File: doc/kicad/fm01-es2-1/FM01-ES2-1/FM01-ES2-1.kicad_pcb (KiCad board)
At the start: 2 copper layers, 20 x 32 mm, 27 parts, among them J1 USB_B_Micro, J2 Conn_01x10, J3 Conn_01x10, J4 Conn_01x30, U1 ESP32-S2-WROVER-I

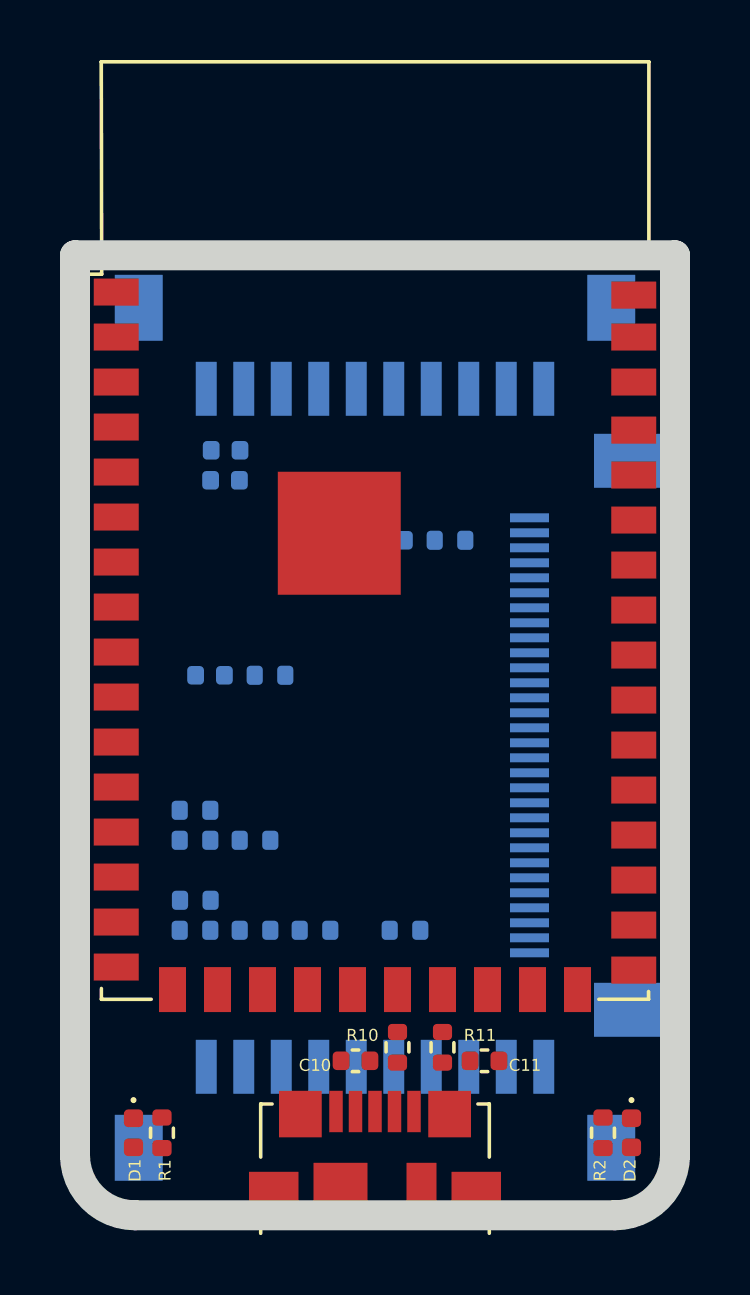
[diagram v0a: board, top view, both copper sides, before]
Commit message: doc/kicad: FM01-ES2-1  update PCB
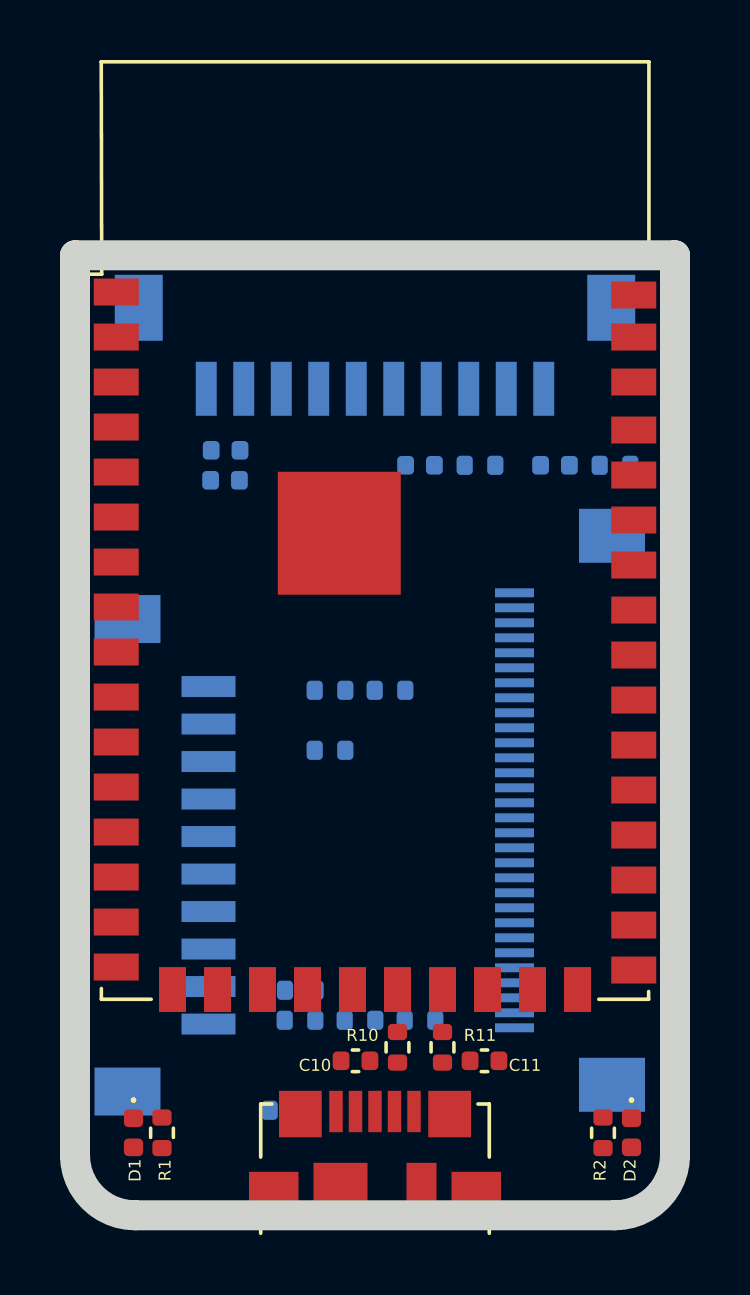
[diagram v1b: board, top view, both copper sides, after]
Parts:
- moved J3 11.0 mm to (183.0, 88.0), turned to 90 degrees
- moved C3 9.90 mm to (191.5, 75.0)
- moved R3 9.90 mm to (193.5, 75.0)
- moved R18 7.21 mm to (187.0, 96.5)
- moved R33 6.73 mm to (188.5, 82.5)
- moved R34 6.73 mm to (190.5, 82.5)
- moved C4 6.04 mm to (196.0, 75.0)
- moved R4 6.04 mm to (198.0, 75.0)
- moved R35 4.92 mm to (188.5, 84.5)
- moved R30 4.61 mm to (187.5, 93.5)
- moved R31 4.61 mm to (189.5, 93.5)
- moved R32 4.61 mm to (191.5, 93.5)
- moved R36 4.61 mm to (187.5, 92.5)
- moved J4 2.55 mm to (196.5, 86.5)
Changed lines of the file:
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@@
     (46 B.CrtYd user)
     (47 F.CrtYd user)
-    (48 B.Fab user hide)
-    (49 F.Fab user hide)
+    (48 B.Fab user)
+    (49 F.Fab user)
   )
   (setup
@@
   )
   (module Resistor_SMD:R_0402_1005Metric (layer B.Cu)
-    (at 184.01 89.5)
+    (at 187.51 92.5)
     (descr "Resistor SMD 0402 (1005 Metric), square (rectangular) end terminal, IPC_7351 nominal, (Body size source: IPC-SM-782 page 72, https://www.pcb-3d.com/wordpress/wp-content/uploads/ipc-sm-782a_amendment_1_and_2.pdf), generated with kicad-footprint-generator")
     (tags resistor)
     (attr smd)
-    (fp_text reference R36 (at -1.51 0) (layer B.SilkS)
+    (fp_text reference R36 (at -0.01 -1) (layer B.SilkS)
       (effects (font (size 0.4 0.4) (thickness 0.1)) (justify mirror))
     )
@@
   )
   (module Resistor_SMD:R_0402_1005Metric (layer B.Cu)
-    (at 184 86.5)
+    (at 188.5 84.5)
     (descr "Resistor SMD 0402 (1005 Metric), square (rectangular) end terminal, IPC_7351 nominal, (Body size source: IPC-SM-782 page 72, https://www.pcb-3d.com/wordpress/wp-content/uploads/ipc-sm-782a_amendment_1_and_2.pdf), generated with kicad-footprint-generator")
     (tags resistor)
     (attr smd)
-    (fp_text reference R35 (at 0 2) (layer B.SilkS)
+    (fp_text reference R35 (at 0 1) (layer B.SilkS)
       (effects (font (size 0.4 0.4) (thickness 0.1)) (justify mirror))
     )
@@
   )
   (module Resistor_SMD:R_0402_1005Metric (layer B.Cu)
-    (at 186 87.5 180)
+    (at 190.5 82.5 180)
     (descr "Resistor SMD 0402 (1005 Metric), square (rectangular) end terminal, IPC_7351 nominal, (Body size source: IPC-SM-782 page 72, https://www.pcb-3d.com/wordpress/wp-content/uploads/ipc-sm-782a_amendment_1_and_2.pdf), generated with kicad-footprint-generator")
     (tags resistor)
@@
   )
   (module Resistor_SMD:R_0402_1005Metric (layer B.Cu)
-    (at 184 87.5 180)
+    (at 188.5 82.5 180)
     (descr "Resistor SMD 0402 (1005 Metric), square (rectangular) end terminal, IPC_7351 nominal, (Body size source: IPC-SM-782 page 72, https://www.pcb-3d.com/wordpress/wp-content/uploads/ipc-sm-782a_amendment_1_and_2.pdf), generated with kicad-footprint-generator")
     (tags resistor)
     (attr smd)
-    (fp_text reference R33 (at 1.5 1) (layer B.SilkS)
+    (fp_text reference R33 (at 0 -1) (layer B.SilkS)
       (effects (font (size 0.4 0.4) (thickness 0.1)) (justify mirror))
     )
@@
   )
   (module Resistor_SMD:R_0402_1005Metric (layer B.Cu)
-    (at 188 90.5 180)
+    (at 191.5 93.5 180)
     (descr "Resistor SMD 0402 (1005 Metric), square (rectangular) end terminal, IPC_7351 nominal, (Body size source: IPC-SM-782 page 72, https://www.pcb-3d.com/wordpress/wp-content/uploads/ipc-sm-782a_amendment_1_and_2.pdf), generated with kicad-footprint-generator")
     (tags resistor)
@@
   )
   (module Resistor_SMD:R_0402_1005Metric (layer B.Cu)
-    (at 186 90.5 180)
+    (at 189.5 93.5 180)
     (descr "Resistor SMD 0402 (1005 Metric), square (rectangular) end terminal, IPC_7351 nominal, (Body size source: IPC-SM-782 page 72, https://www.pcb-3d.com/wordpress/wp-content/uploads/ipc-sm-782a_amendment_1_and_2.pdf), generated with kicad-footprint-generator")
     (tags resistor)
@@
   )
   (module Resistor_SMD:R_0402_1005Metric (layer B.Cu)
-    (at 184 90.5)
+    (at 187.5 93.5)
     (descr "Resistor SMD 0402 (1005 Metric), square (rectangular) end terminal, IPC_7351 nominal, (Body size source: IPC-SM-782 page 72, https://www.pcb-3d.com/wordpress/wp-content/uploads/ipc-sm-782a_amendment_1_and_2.pdf), generated with kicad-footprint-generator")
     (tags resistor)
@@
   )
   (module Resistor_SMD:R_0402_1005Metric (layer B.Cu)
-    (at 191 90.5)
+    (at 187 96.5)
     (descr "Resistor SMD 0402 (1005 Metric), square (rectangular) end terminal, IPC_7351 nominal, (Body size source: IPC-SM-782 page 72, https://www.pcb-3d.com/wordpress/wp-content/uploads/ipc-sm-782a_amendment_1_and_2.pdf), generated with kicad-footprint-generator")
     (tags resistor)
@@
   )
   (module Resistor_SMD:R_0402_1005Metric (layer B.Cu)
-    (at 192.5 77.5)
+    (at 198 75)
     (descr "Resistor SMD 0402 (1005 Metric), square (rectangular) end terminal, IPC_7351 nominal, (Body size source: IPC-SM-782 page 72, https://www.pcb-3d.com/wordpress/wp-content/uploads/ipc-sm-782a_amendment_1_and_2.pdf), generated with kicad-footprint-generator")
     (tags resistor)
@@
   )
   (module Resistor_SMD:R_0402_1005Metric (layer B.Cu)
-    (at 186.5 82)
+    (at 193.5 75)
     (descr "Resistor SMD 0402 (1005 Metric), square (rectangular) end terminal, IPC_7351 nominal, (Body size source: IPC-SM-782 page 72, https://www.pcb-3d.com/wordpress/wp-content/uploads/ipc-sm-782a_amendment_1_and_2.pdf), generated with kicad-footprint-generator")
     (tags resistor)
@@
   )
   (module Connector_FFC-FPC:Hirose_FH12-30S-0.5SH_1x30-1MP_P0.50mm_Horizontal (layer B.Cu)
-    (at 197 84 270)
+    (at 196.5 86.5 270)
     (descr "Hirose FH12, FFC/FPC connector, FH12-30S-0.5SH, 30 Pins per row (https://www.hirose.com/product/en/products/FH12/FH12-24S-0.5SH(55)/), generated with kicad-footprint-generator")
     (tags "connector Hirose FH12 horizontal")
@@
   )
   (module Connector_Hirose:Hirose_DF13C_CL535-0410-4-51_1x10-1MP_P1.25mm_Vertical (layer B.Cu)
-    (at 190 96.5 180)
+    (at 183 88 90)
     (descr "Hirose DF13C SMD, CL535-0410-4-51, 10 Pins per row (https://www.hirose.com/product/en/products/DF13/DF13C-10P-1.25V%2851%29/), generated with kicad-footprint-generator")
     (tags "connector Hirose DF13C vertical")
     (attr smd)
-    (fp_text reference J3 (at 0.5 3) (layer B.SilkS) hide
-      (effects (font (size 0.4 0.4) (thickness 0.1)) (justify mirror))
-    )
-    (fp_text value Conn_01x10 (at 0 -4.15) (layer B.Fab)
+    (fp_text reference J3 (at 0.5 3 90) (layer B.SilkS) hide
+      (effects (font (size 0.4 0.4) (thickness 0.1)) (justify mirror))
+    )
+    (fp_text value Conn_01x10 (at 0 -4.15 90) (layer B.Fab)
       (effects (font (size 1 1) (thickness 0.15)) (justify mirror))
     )
-    (fp_text user %R (at 0 -2.25) (layer B.Fab)
-      (effects (font (size 0.4 0.4) (thickness 0.1)) (justify mirror))
-    )
-    (fp_text user KEEPOUT (at 0 -0.735) (layer Cmts.User)
+    (fp_text user %R (at 0 -2.25 90) (layer B.Fab)
+      (effects (font (size 0.4 0.4) (thickness 0.1)) (justify mirror))
+    )
+    (fp_text user KEEPOUT (at 0 -0.735 90) (layer Cmts.User)
       (effects (font (size 1 1) (thickness 0.15)))
     )
@@
     (fp_line (start 9.18 -3.45) (end 9.18 2.85) (layer B.CrtYd) (width 0.05))
     (fp_line (start 9.18 2.85) (end -9.18 2.85) (layer B.CrtYd) (width 0.05))
-    (pad 10 smd rect (at 5.625 1.45 180) (size 0.7 1.8) (layers B.Cu B.Paste B.Mask)
+    (pad 10 smd rect (at 5.625 1.45 90) (size 0.7 1.8) (layers B.Cu B.Paste B.Mask)
       (net 20 /VBAT))
-    (pad 9 smd rect (at 4.375 1.45 180) (size 0.7 1.8) (layers B.Cu B.Paste B.Mask)
-      (net 1 GND))
-    (pad 8 smd rect (at 3.125 1.45 180) (size 0.7 1.8) (layers B.Cu B.Paste B.Mask)
+    (pad 9 smd rect (at 4.375 1.45 90) (size 0.7 1.8) (layers B.Cu B.Paste B.Mask)
+      (net 1 GND))
+    (pad 8 smd rect (at 3.125 1.45 90) (size 0.7 1.8) (layers B.Cu B.Paste B.Mask)
       (net 21 /IO18))
-    (pad 7 smd rect (at 1.875 1.45 180) (size 0.7 1.8) (layers B.Cu B.Paste B.Mask)
+    (pad 7 smd rect (at 1.875 1.45 90) (size 0.7 1.8) (layers B.Cu B.Paste B.Mask)
       (net 22 /IO17))
-    (pad 6 smd rect (at 0.625 1.45 180) (size 0.7 1.8) (layers B.Cu B.Paste B.Mask)
+    (pad 6 smd rect (at 0.625 1.45 90) (size 0.7 1.8) (layers B.Cu B.Paste B.Mask)
       (net 23 /IO16))
-    (pad 5 smd rect (at -0.625 1.45 180) (size 0.7 1.8) (layers B.Cu B.Paste B.Mask)
+    (pad 5 smd rect (at -0.625 1.45 90) (size 0.7 1.8) (layers B.Cu B.Paste B.Mask)
       (net 24 /IO15))
-    (pad 4 smd rect (at -1.875 1.45 180) (size 0.7 1.8) (layers B.Cu B.Paste B.Mask)
+    (pad 4 smd rect (at -1.875 1.45 90) (size 0.7 1.8) (layers B.Cu B.Paste B.Mask)
       (net 25 /IO14))
-    (pad 3 smd rect (at -3.125 1.45 180) (size 0.7 1.8) (layers B.Cu B.Paste B.Mask)
+    (pad 3 smd rect (at -3.125 1.45 90) (size 0.7 1.8) (layers B.Cu B.Paste B.Mask)
       (net 26 /IO13))
-    (pad 2 smd rect (at -4.375 1.45 180) (size 0.7 1.8) (layers B.Cu B.Paste B.Mask)
-      (net 1 GND))
-    (pad 1 smd rect (at -5.625 1.45 180) (size 0.7 1.8) (layers B.Cu B.Paste B.Mask)
+    (pad 2 smd rect (at -4.375 1.45 90) (size 0.7 1.8) (layers B.Cu B.Paste B.Mask)
+      (net 1 GND))
+    (pad 1 smd rect (at -5.625 1.45 90) (size 0.7 1.8) (layers B.Cu B.Paste B.Mask)
       (net 27 /VI))
-    (pad MP smd rect (at -7.875 -1.25 180) (size 1.6 2.2) (layers B.Cu B.Paste B.Mask))
-    (pad MP smd rect (at 7.875 -1.25 180) (size 1.6 2.2) (layers B.Cu B.Paste B.Mask))
+    (pad MP smd rect (at -7.875 -1.25 90) (size 1.6 2.2) (layers B.Cu B.Paste B.Mask))
+    (pad MP smd rect (at 7.875 -1.25 90) (size 1.6 2.2) (layers B.Cu B.Paste B.Mask))
     (model ${KISYS3DMOD}/Connector_Hirose.3dshapes/Hirose_DF13C_CL535-0410-4-51_1x10-1MP_P1.25mm_Vertical.wrl
       (at (xyz 0 0 0))
@@
   )
   (module Capacitor_SMD:C_0402_1005Metric (layer B.Cu)
-    (at 190.5 77.5)
+    (at 196 75)
     (descr "Capacitor SMD 0402 (1005 Metric), square (rectangular) end terminal, IPC_7351 nominal, (Body size source: IPC-SM-782 page 76, https://www.pcb-3d.com/wordpress/wp-content/uploads/ipc-sm-782a_amendment_1_and_2.pdf), generated with kicad-footprint-generator")
     (tags capacitor)
@@
   )
   (module Capacitor_SMD:C_0402_1005Metric (layer B.Cu)
-    (at 184.5 82)
+    (at 191.5 75)
     (descr "Capacitor SMD 0402 (1005 Metric), square (rectangular) end terminal, IPC_7351 nominal, (Body size source: IPC-SM-782 page 76, https://www.pcb-3d.com/wordpress/wp-content/uploads/ipc-sm-782a_amendment_1_and_2.pdf), generated with kicad-footprint-generator")
     (tags capacitor)
